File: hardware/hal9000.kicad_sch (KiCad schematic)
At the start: 13 parts

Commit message: hw: reva2 kicad files
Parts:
- C2: footprint Capacitor_SMD:C_0805_2012Metric_Pad1.18x1.45mm_HandSolder -> Capacitor_THT:CP_Radial_D6.3mm_P2.50mm
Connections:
- net +3V3: now also J_PHOTON_R1.1 (Pin_1); no longer J_PHOTON_R1.12 (Pin_12)
- net D0: now also J_PHOTON_R1.12 (Pin_12), R1.2
- net D3: now also J_BUTTON1.1 (Pin_1), J_PHOTON_R1.8 (Pin_8)
- net at J_PHOTON_R1.4 (Pin_4): no longer J_BUTTON1.1 (Pin_1)
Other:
- moved on the sheet: J_PHOTON_R1
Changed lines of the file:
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@@
 	(wire
 		(pts
-			(xy 180.34 121.92) (xy 167.64 121.92)
+			(xy 180.34 119.38) (xy 167.64 119.38)
 		)
 		(stroke
@@
 	(wire
 		(pts
-			(xy 107.95 140.97) (xy 121.92 140.97)
+			(xy 167.64 129.54) (xy 171.45 129.54)
 		)
 		(stroke
@@
 	(wire
 		(pts
-			(xy 109.22 80.01) (xy 109.22 85.09)
+			(xy 107.95 140.97) (xy 121.92 140.97)
 		)
 		(stroke
@@
 	(wire
 		(pts
-			(xy 129.54 114.3) (xy 140.97 114.3)
+			(xy 109.22 80.01) (xy 109.22 85.09)
 		)
 		(stroke
@@
 	(wire
 		(pts
-			(xy 167.64 129.54) (xy 171.45 129.54)
+			(xy 129.54 114.3) (xy 140.97 114.3)
 		)
 		(stroke
@@
 	(wire
 		(pts
-			(xy 180.34 152.4) (xy 180.34 121.92)
+			(xy 180.34 152.4) (xy 180.34 119.38)
 		)
 		(stroke
@@
 	)
 	(label "D0"
-		(at 165.1 129.54 0)
+		(at 167.64 129.54 0)
 		(effects
 			(font
@@
 	)
 	(label "D3"
-		(at 165.1 121.92 0)
+		(at 167.64 119.38 0)
 		(effects
 			(font
@@
 		)
 		(property "Value" "+3V3"
-			(at 171.45 101.5999 90)
+			(at 170.18 101.6 90)
 			(effects
 				(font
@@
 			)
 		)
-		(property "Footprint" "Capacitor_SMD:C_0805_2012Metric_Pad1.18x1.45mm_HandSolder"
+		(property "Footprint" "Capacitor_THT:CP_Radial_D6.3mm_P2.50mm"
 			(at 79.7052 134.62 0)
 			(effects
@@
 			)
 		)
-		(property "Description" "Unpolarized capacitor"
+		(property "Description" ""
 			(at 78.74 130.81 0)
 			(effects
@@
 	(symbol
 		(lib_id "Connector_Generic:Conn_01x12")
-		(at 162.56 116.84 180)
-		(unit 1)
-		(exclude_from_sim no)
-		(in_bom yes)
-		(on_board yes)
-		(dnp no)
-		(fields_autoplaced yes)
+		(at 162.56 114.3 0)
+		(mirror y)
+		(unit 1)
+		(exclude_from_sim no)
+		(in_bom yes)
+		(on_board yes)
+		(dnp no)
 		(property "Reference" "J_PHOTON_R1"
-			(at 162.56 95.25 0)
+			(at 162.814 93.98 0)
 			(effects
 				(font
@@
 		)
 		(property "Value" "Conn_01x12"
-			(at 162.56 97.79 0)
+			(at 162.052 96.52 0)
 			(effects
 				(font
@@
 		)
 		(property "Footprint" "Connector_PinSocket_2.54mm:PinSocket_1x12_P2.54mm_Vertical"
-			(at 162.56 116.84 0)
+			(at 162.56 114.3 0)
 			(effects
 				(font
@@
 		)
 		(property "Datasheet" "~"
-			(at 162.56 116.84 0)
+			(at 162.56 114.3 0)
 			(effects
 				(font
@@
 		)
 		(property "Description" "Generic connector, single row, 01x12, script generated (kicad-library-utils/schlib/autogen/connector/)"
-			(at 162.56 116.84 0)
-			(effects
-				(font
+			(at 162.56 114.3 0)
+			(effects
+				(font

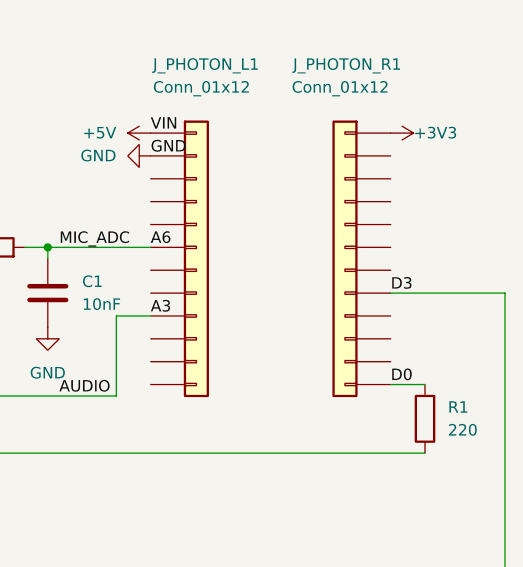
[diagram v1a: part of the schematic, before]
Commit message: Update hw/fw to match reva2 and reva3 pushbutton at D4
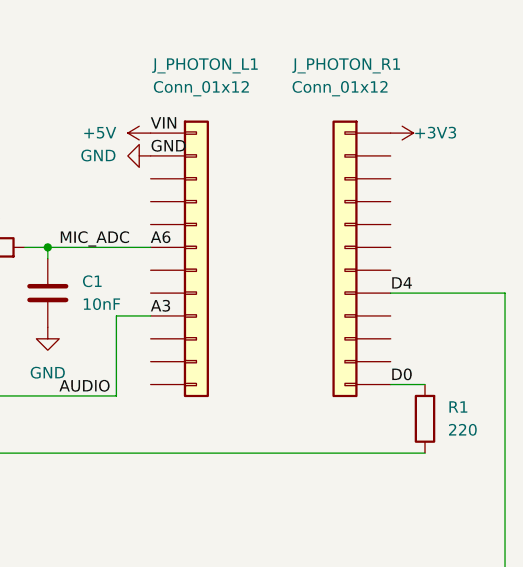
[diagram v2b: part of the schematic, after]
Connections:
- net D3 renamed D4
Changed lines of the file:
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@@
 		)
 	)
-	(label "D3"
+	(label "D4"
 		(at 167.64 119.38 0)
 		(effects
